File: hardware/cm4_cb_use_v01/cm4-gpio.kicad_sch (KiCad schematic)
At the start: 12 parts, among them J1 DNP, J2 USB4105-GF-A, U1 74LVC1G07SE-7

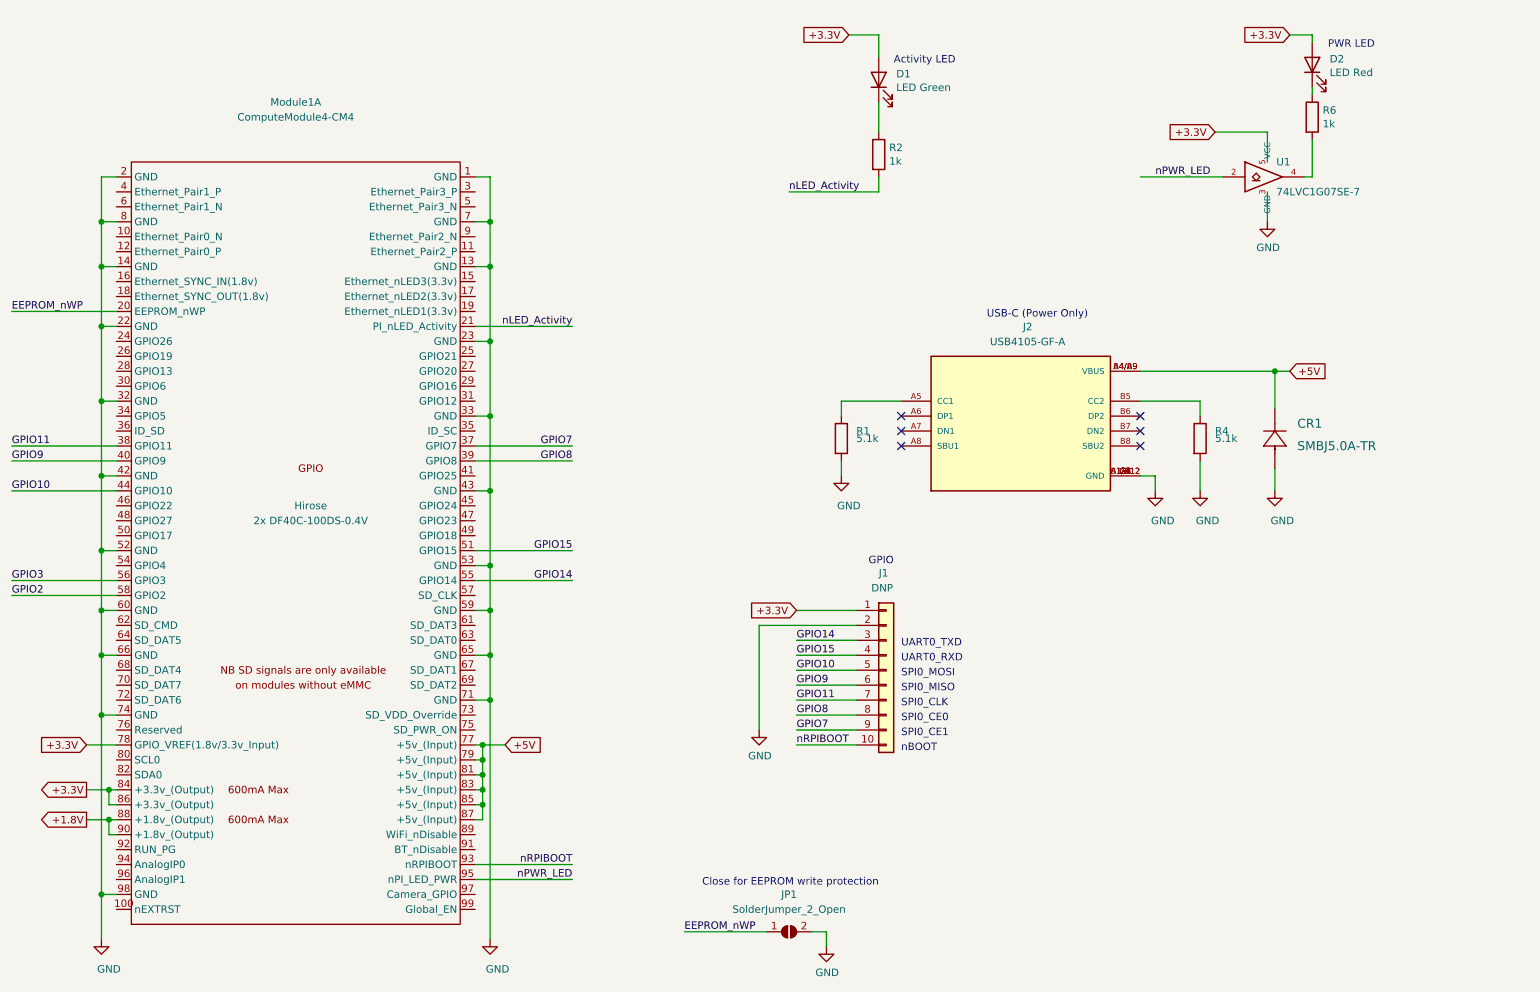
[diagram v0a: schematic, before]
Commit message: added usb-c and hdmi
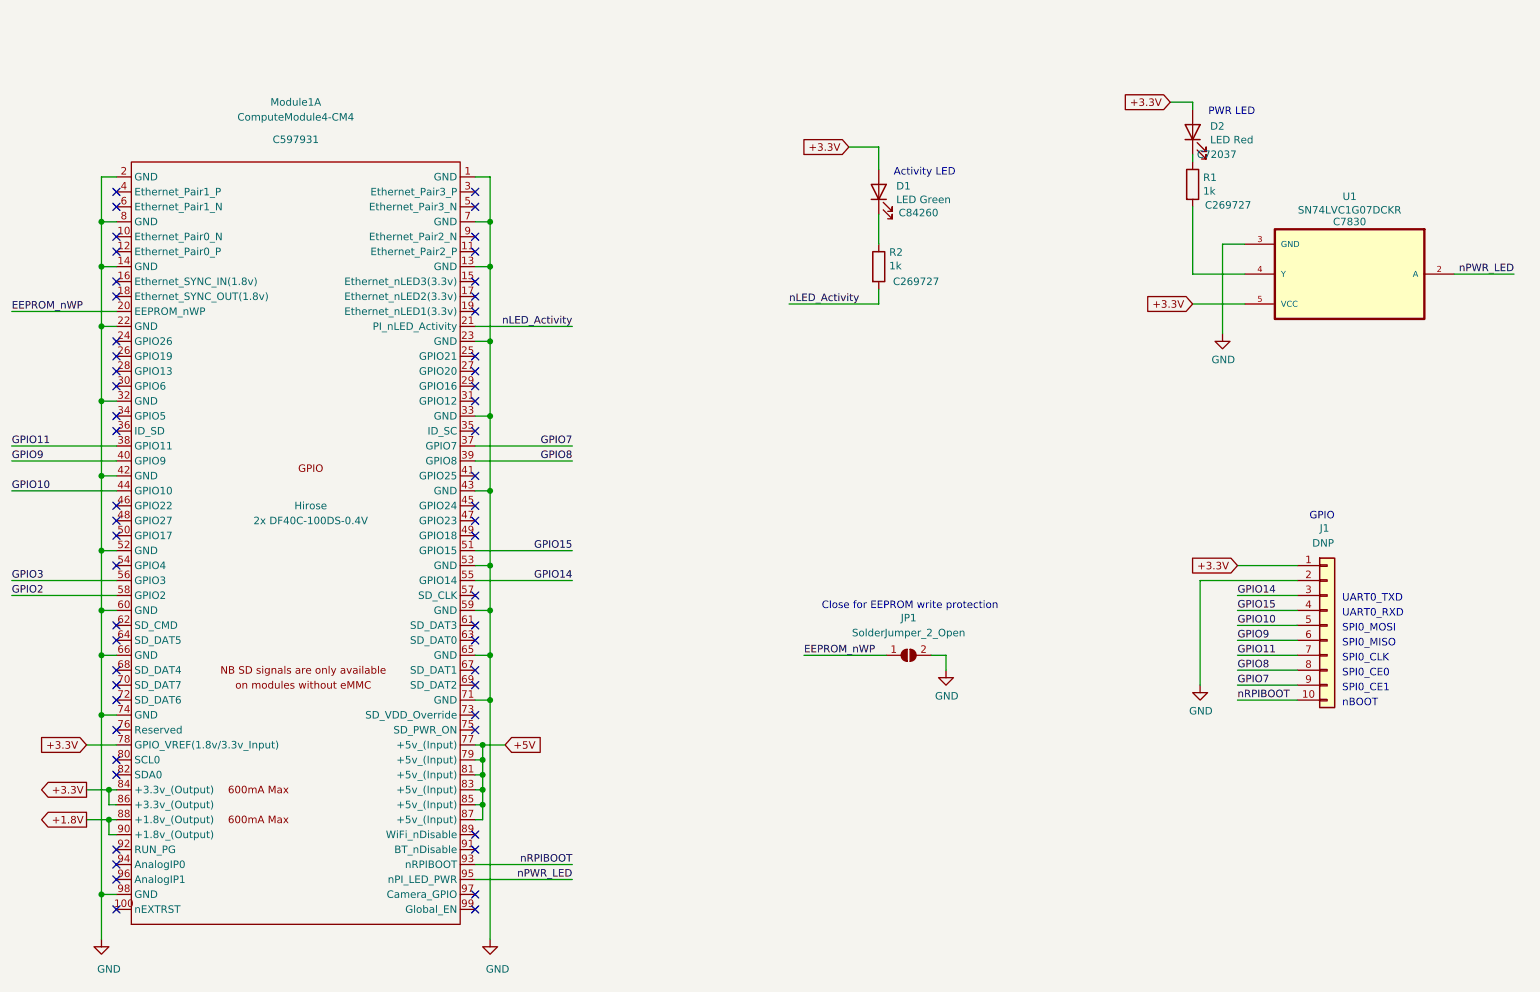
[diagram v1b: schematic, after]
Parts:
- removed CR1: SMBJ5.0A-TR, footprints:SMBJ5.0A-TR, symbol 2020-11-06_22-01-36:SMBJ5.0A-TR
- removed J2: USB4105-GF-A, USB4105-GF-A:GCT_USB4105-GF-A, symbol USB4105-GF-A:USB4105-GF-A
- removed R4: 5.1k, Resistor_SMD:R_0603_1608Metric_Pad0.98x0.95mm_HandSolder, symbol Device:R
- removed R6: 1k, Resistor_SMD:R_0603_1608Metric_Pad0.98x0.95mm_HandSolder, symbol Device:R
- removed U1: 74LVC1G07SE-7, Package_TO_SOT_SMD:SOT-353_SC-70-5, symbol CM4IO:74LVC1G07_copy
- added U1: SN74LVC1G07DCKR, symbol SN74LVC1G07DCKR:SN74LVC1G07DCKR
- D1: footprint LED_SMD:LED_0603_1608Metric -> LED_SMD:LED_0805_2012Metric; Digi-Key_PN 160-1478-1-ND -> (none); LCSC (none) -> C84260; MPN LTST-S270KGKT -> NCD0805G1; Manufacturer Lite-On Inc. -> Foshan NationStar Optoelectronics; Part Description Green 572nm LED Indication - Discrete 2.2V 2-SMD, No Lead -> Green 525~537.5nm 0805 Light Emitting Diodes (LED) RoHS
- D2: footprint LED_SMD:LED_0603_1608Metric -> LED_SMD:LED_0805_2012Metric; Digi-Key_PN 160-1479-1-ND -> (none); LCSC (none) -> C72037; MPN LTST-S270KRKT -> 17-21SURC/S530-A3/TR8; Manufacturer Lite-On Inc. -> Everlight Elec; Part Description Red 620nm LED Indication - Discrete 2.2V 2-SMD, No Lead -> Red 624~632nm 0805 Light Emitting Diodes (LED) RoHS
- Module1: LCSC (none) -> C597931
- R1: value 5.1k -> 1k; footprint Resistor_SMD:R_0603_1608Metric_Pad0.98x0.95mm_HandSolder -> Resistor_SMD:R_0805_2012Metric; Digi-Key_PN 311-5.10KHRCT-ND -> (none); LCSC (none) -> C269727; MPN RC0603FR-075K1L -> RMC08051K5%N; Manufacturer Yageo -> TyoHM
- R2: footprint Resistor_SMD:R_0603_1608Metric_Pad0.98x0.95mm_HandSolder -> Resistor_SMD:R_0805_2012Metric; Digi-Key_PN 311-1.00KHRCT-ND -> (none); LCSC (none) -> C269727; MPN RC0603FR-071KL -> RMC08051K5%N; Manufacturer Yageo -> TyoHM
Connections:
- net +3.3V: now also U1.5 (VCC)
- net GND: now also U1.3 (GND); no longer R1.2
- net nPWR_LED: now also U1.2 (A)
- net at D2.1 (K): now also R1.1
- new net: R1.2, U1.4 (Y)
- no-connect marks 6 -> 55
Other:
- note removed: "USB-C (Power Only)"
- moved on the sheet: D1, D2, J1, JP1, R2

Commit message: added some 3d models
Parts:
- U1: footprint (none) -> SN74LVC1G07DCKR:SOT65P210X110-5N
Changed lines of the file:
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@@
     (property "Reference" "U1" (id 0) (at 252.73 49.0536 0))
     (property "Value" "SN74LVC1G07DCKR" (id 1) (at 252.73 51.3523 0))
-    (property "Footprint" "" (id 2) (at 252.73 62.23 0)
+    (property "Footprint" "SN74LVC1G07DCKR:SOT65P210X110-5N" (id 2) (at 252.73 62.23 0)
       (effects (font (size 1.27 1.27)) (justify left bottom) hide)
     )
@@
       (effects (font (size 1.27 1.27)) hide)
     )
-    (property "LCSC" "C597931" (id 8) (at 73.66 39.37 0))
+    (property "LCSC" "C597931" (id 4) (at 73.66 39.37 0))
     (pin "1")
     (pin "10")

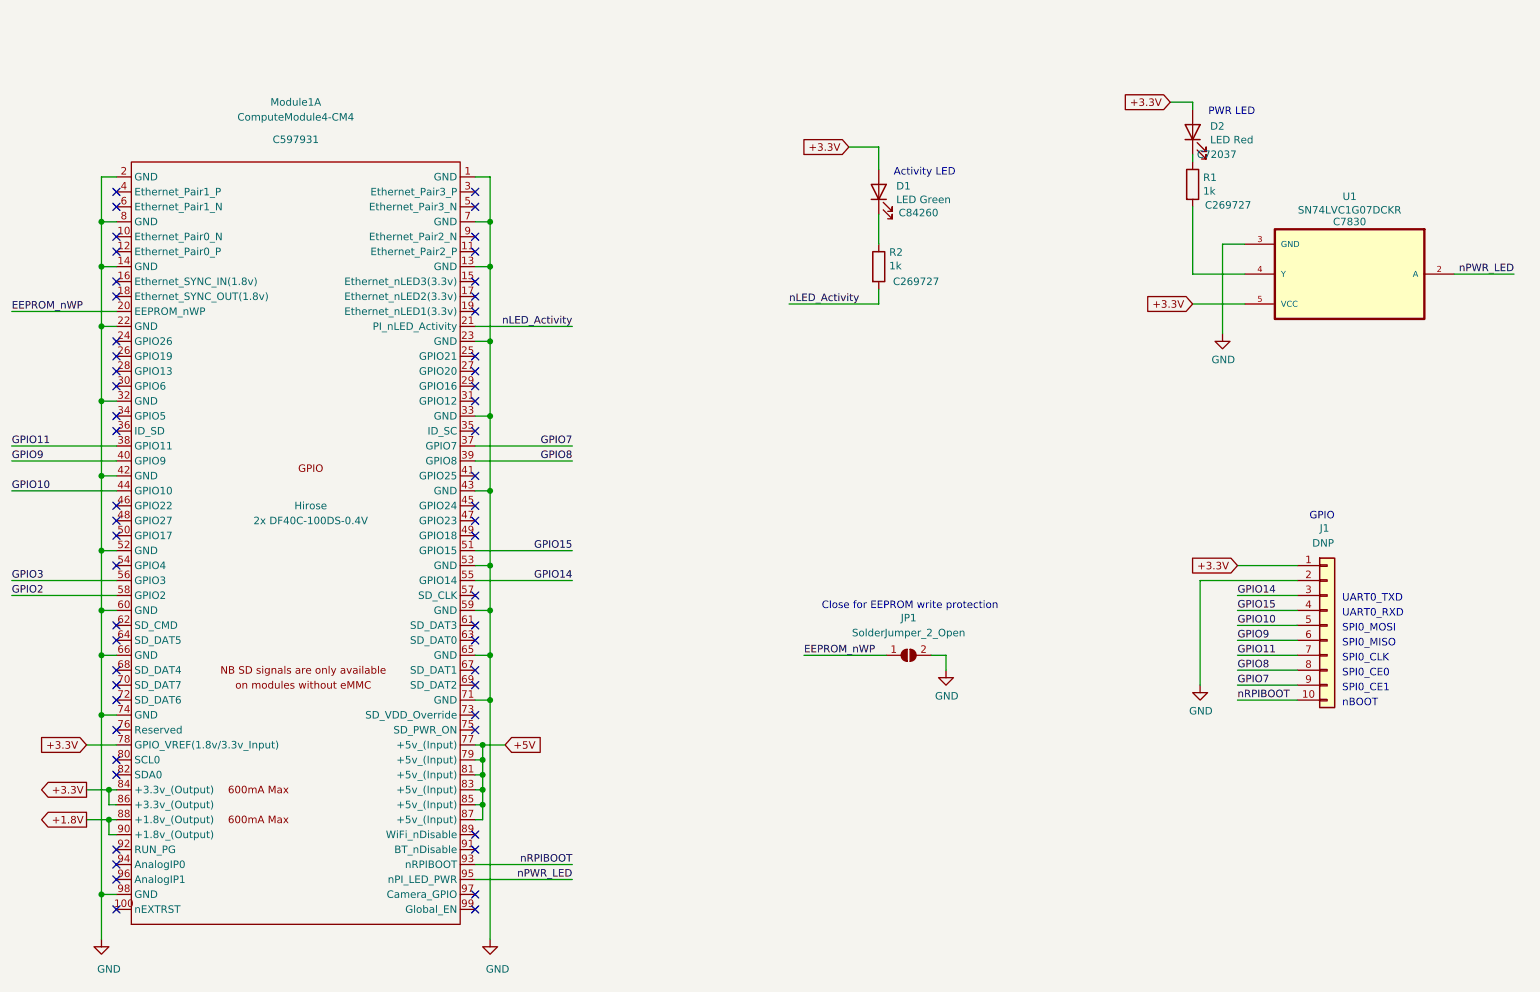
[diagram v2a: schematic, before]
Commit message: added 3d models and started pcb layout
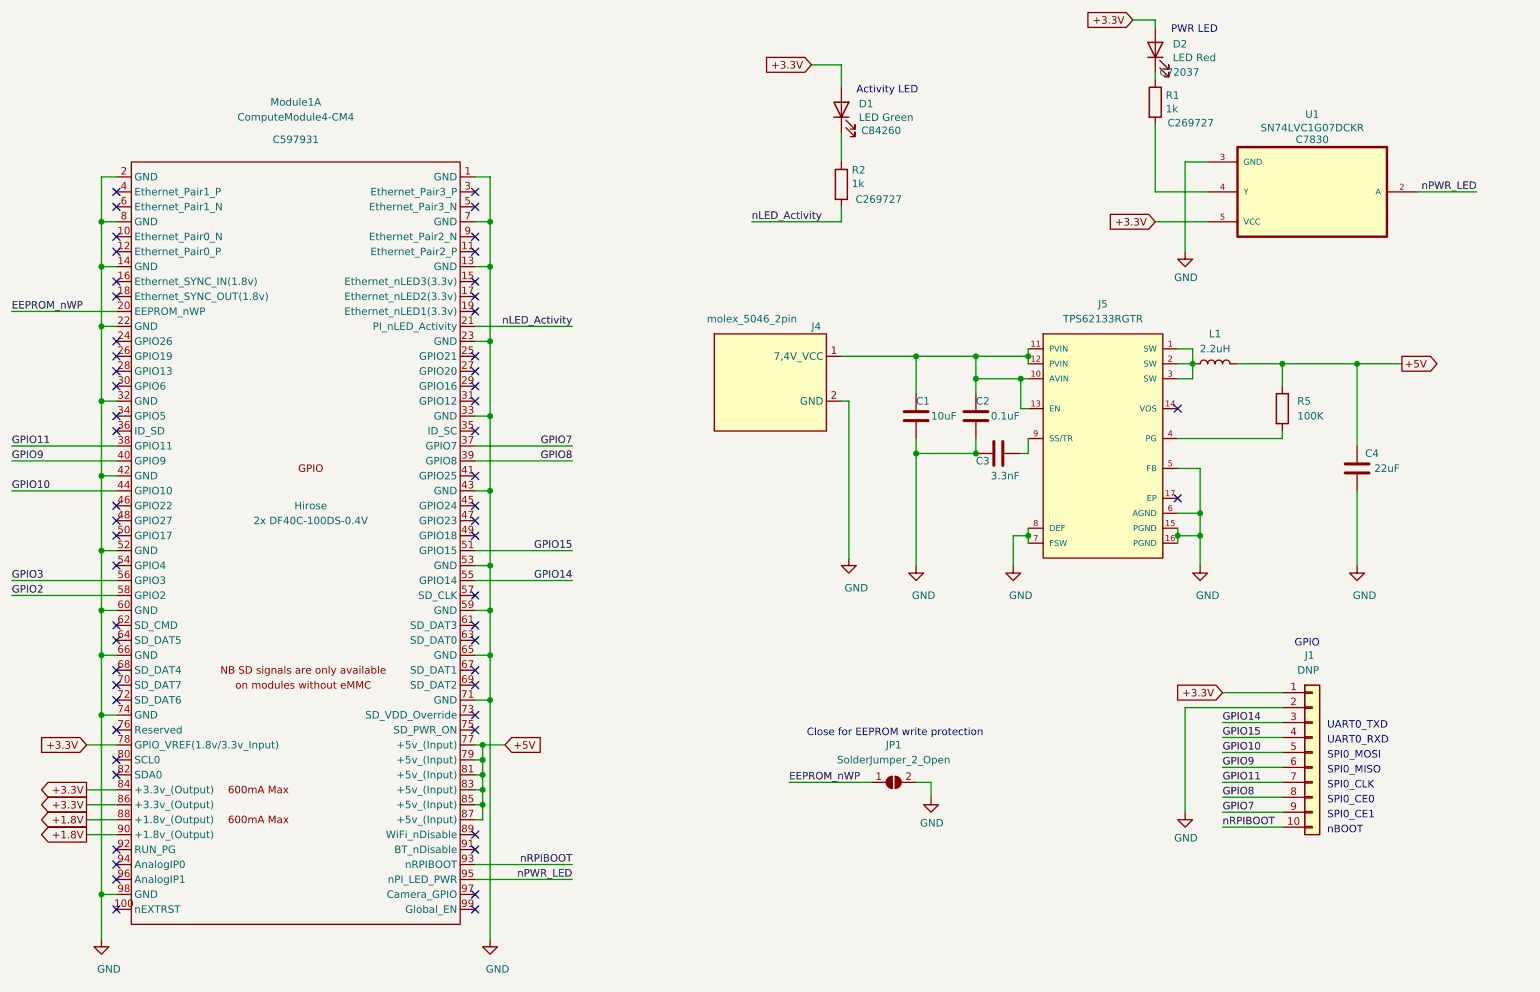
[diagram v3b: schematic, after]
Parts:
- added C1: 10uF, Capacitor_SMD:C_0805_2012Metric, symbol Device:C
- added C2: 0.1uF, Capacitor_SMD:C_0805_2012Metric, symbol Device:C
- added C3: 3.3nF, Capacitor_SMD:C_0805_2012Metric, symbol Device:C
- added C4: 22uF, Capacitor_SMD:C_0805_2012Metric, symbol Device:C
- added J4: molex_5046_2pin, Connector_Molex:Molex_KK-254_AE-6410-02A_1x02_P2.54mm_Vertical, symbol molex_5046_2pin:molex_5046_2pin
- added J5: TPS62133RGTR, TPS62133:Texas_Instruments-TPS62133RGTR-Manufacturer_Recommended, symbol TPS62133:TPS62133RGTR
- added L1: 2.2uH, Inductor_SMD:L_0805_2012Metric, symbol Device:L
- added R5: 100K, Resistor_SMD:R_0805_2012Metric, symbol Device:R
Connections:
- net +5V: now also C4.1, L1.2, R5.1
- net GND: now also C1.2, C2.2, C3.2, C4.2, J4.2 (GND), J5.15 (PGND), J5.16 (PGND), J5.5 (FB), J5.6 (AGND), J5.7 (FSW), J5.8 (DEF)
- new net: C1.1, C2.1, J4.1 (7,4V_VCC), J5.10 (AVIN), J5.11 (PVIN), J5.12 (PVIN), J5.13 (EN)
- new net: C3.1, J5.9 (SS/TR)
- new net: J5.1 (SW), J5.2 (SW), J5.3 (SW), L1.1
- new net: J5.4 (PG), R5.2
- no-connect marks 55 -> 57
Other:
- moved on the sheet: D1, D2, J1, JP1, R1, R2, U1
